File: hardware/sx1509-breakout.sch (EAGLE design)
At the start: 33 parts, among them U1 SX1509

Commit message: Adding silk around headers. Labeling SJ1.
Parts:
- removed JP11: (no value), SparkFun-Connectors:M111X11_NO_SILK
- added JP2: (no value), SparkFun-Connectors:M02PTH
- JP1: device SparkFun-Connectors:M021X02_NO_SILK -> SparkFun-Connectors:I2C_STANDARD
- JP3: device SparkFun-Connectors:I2C_STANDARD_NO_SILK -> SparkFun-Connectors:M11PTH
- JP4: value (none) -> IDC-5X2; device SparkFun-Connectors:M021X02_NO_SILK -> SparkFun-Connectors:M05X2SHD-NS
- JP5: value (none) -> IDC-5x2; device SparkFun-Connectors:I2C_STANDARD_NO_SILK -> SparkFun-Connectors:M05X2SHD-NS
- JP6: device SparkFun-Connectors:M111X11_NO_SILK -> SparkFun-Connectors:I2C_STANDARD
- JP7: value IDC-5X2 -> (none); device SparkFun-Connectors:M05X2SHD-NS -> SparkFun-Connectors:M02PTH
- JP8: value IDC-5x2 -> (none); device SparkFun-Connectors:M05X2SHD-NS -> SparkFun-Connectors:M11PTH
- SJ2, SJ3: value JUMPER-PAD-3-2OF3_NC_BY_TRACE_SMALL -> JUMPER-PAD-2-NC_BY_TRACE; device SparkFun-Passives:JUMPER-PAD-3-2OF3_NC_BY_TRACE_SMALL -> SparkFun-Passives:JUMPER-PAD-2-NC_BY_TRACE
- SJ4, SJ5: value JUMPER-PAD-2-NC_BY_TRACE -> JUMPER-PAD-3-2OF3_NC_BY_TRACE_SMALL; device SparkFun-Passives:JUMPER-PAD-2-NC_BY_TRACE -> SparkFun-Passives:JUMPER-PAD-3-2OF3_NC_BY_TRACE_SMALL
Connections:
- net !INT: now also JP2.2, R1.1; no longer JP4.2, R4.1
- net !RESET: now also JP2.1, JP7.1, R3.1; no longer JP1.1, JP4.1, R6.1
- net 0: now also JP3.4, JP5.1; no longer JP6.4, JP8.1
- net 1: now also JP3.5, JP5.2; no longer JP6.5, JP8.2
- net 10: now also JP4.3, JP8.9; no longer JP11.9, JP7.3
- net 11: now also JP4.4, JP8.8; no longer JP11.8, JP7.4
- net 12: now also JP4.7, JP8.7; no longer JP11.7, JP7.7
- net 13: now also JP4.8, JP8.6; no longer JP11.6, JP7.8
- net 14: now also JP4.9, JP8.5; no longer JP11.5, JP7.9
- net 15: now also JP4.10, JP8.4; no longer JP11.4, JP7.10
- net 2: now also JP3.6, JP5.3; no longer JP6.6, JP8.3
- net 3: now also JP3.7, JP5.4; no longer JP6.7, JP8.4
- net 3.3V: now also JP1.2, JP8.2, R1.2, R3.2, SJ2.2, SJ3.2; no longer JP11.2, JP5.2, R2.2, R4.2, SJ4.2, SJ5.2
- net 4: now also JP3.8, JP5.7; no longer JP6.8, JP8.7
- net 5: now also JP3.9, JP5.8; no longer JP6.9, JP8.8
- net 6: now also JP3.10, JP5.9; no longer JP6.10, JP8.9
- net 7: now also JP3.11, JP5.10; no longer JP6.11, JP8.10
- net 8: now also JP4.1, JP8.11; no longer JP11.11, JP7.1
- net 9: now also JP4.2, JP8.10; no longer JP11.10, JP7.2
- net ADDR0: now also SJ4.2; no longer SJ2.2
- net ADDR1: now also SJ5.2; no longer SJ3.2
- net GND: now also JP1.1, JP4.5, JP5.5, JP8.1, SJ4.3, SJ5.3; no longer JP11.1, JP5.1, JP7.5, JP8.5, SJ2.3, SJ3.3
- net N$1: now also R2.2; no longer R1.2
- net N$2: now also R4.2; no longer R3.2
- net N$8: now also R5.1, SJ4.1; no longer R2.1, SJ2.1
- net N$9: now also R6.1, SJ5.1; no longer R5.1, SJ3.1
- net OSCIO: now also JP7.2; no longer JP1.2
- net SCL: now also JP1.4, JP6.4, R2.1; no longer JP3.4, JP5.4, R1.1
- net SDA: now also JP1.3, JP6.3, R4.1; no longer JP3.3, JP5.3, R3.1
- net VCC1: now also JP3.3, JP5.6, SJ2.1; no longer JP6.3, JP8.6, SJ4.1
- net VCC2: now also JP4.6, JP8.3, SJ3.1; no longer JP11.3, JP7.6, SJ5.1
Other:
- note added: "SJ4 and SJ5 set the I2c address of the SX1509."
- note added: "The VCC1/2 jumpers (SJ2, SJ3) set those pins to 3.3V."
- note removed: "SJ2 and SJ3 set the I2c address of the SX1509."
- note removed: "The VCC1/2 jumpers (SJ4, SJ5) set those pins to 3.3V."
- moved on the sheet: R1, R2, R3, R4, R5, R6

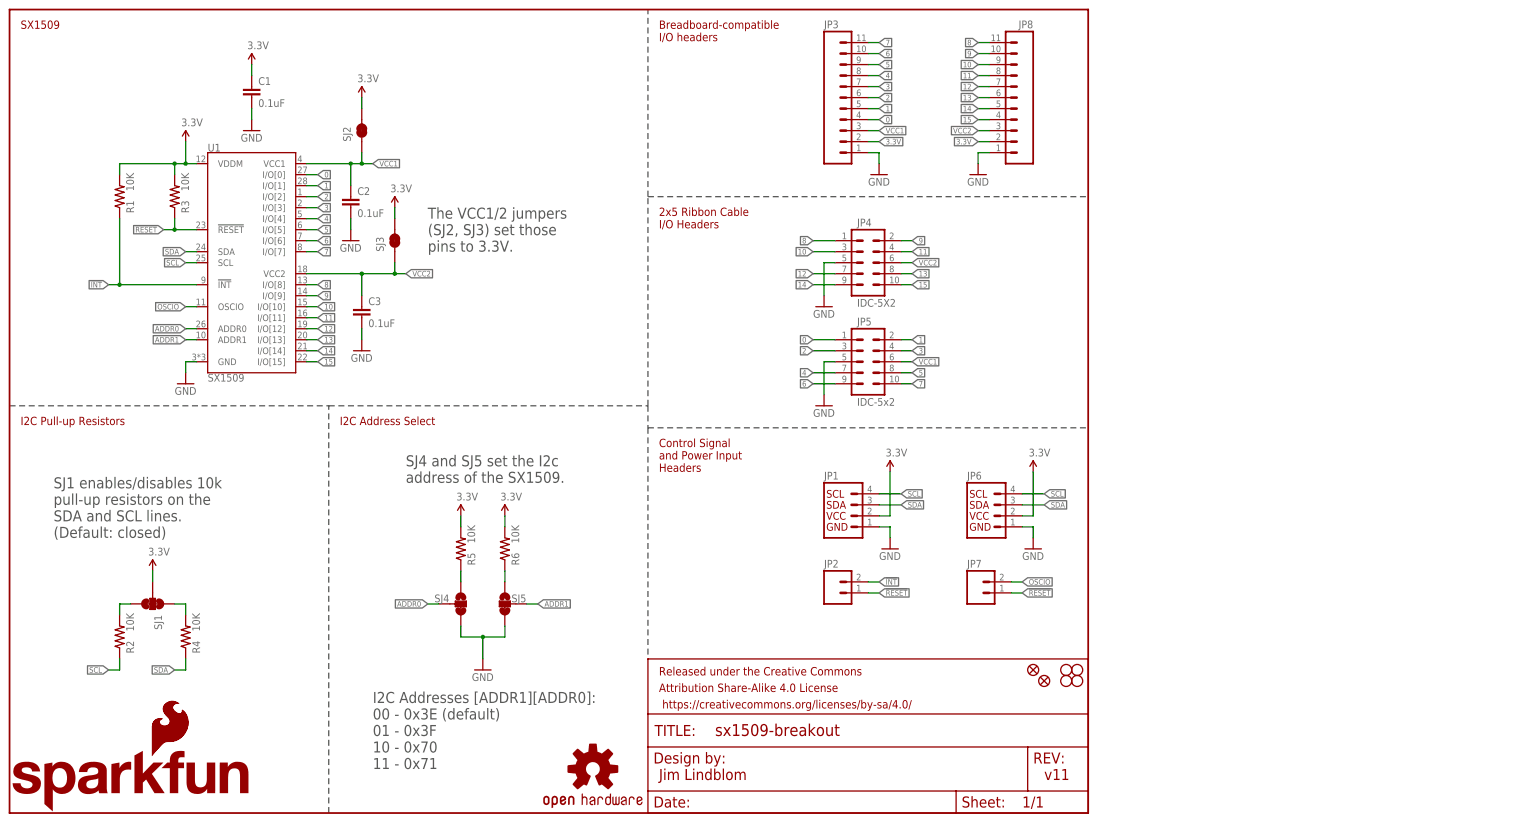
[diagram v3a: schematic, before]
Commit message: Revising GPIO headers to single 2x10 header.
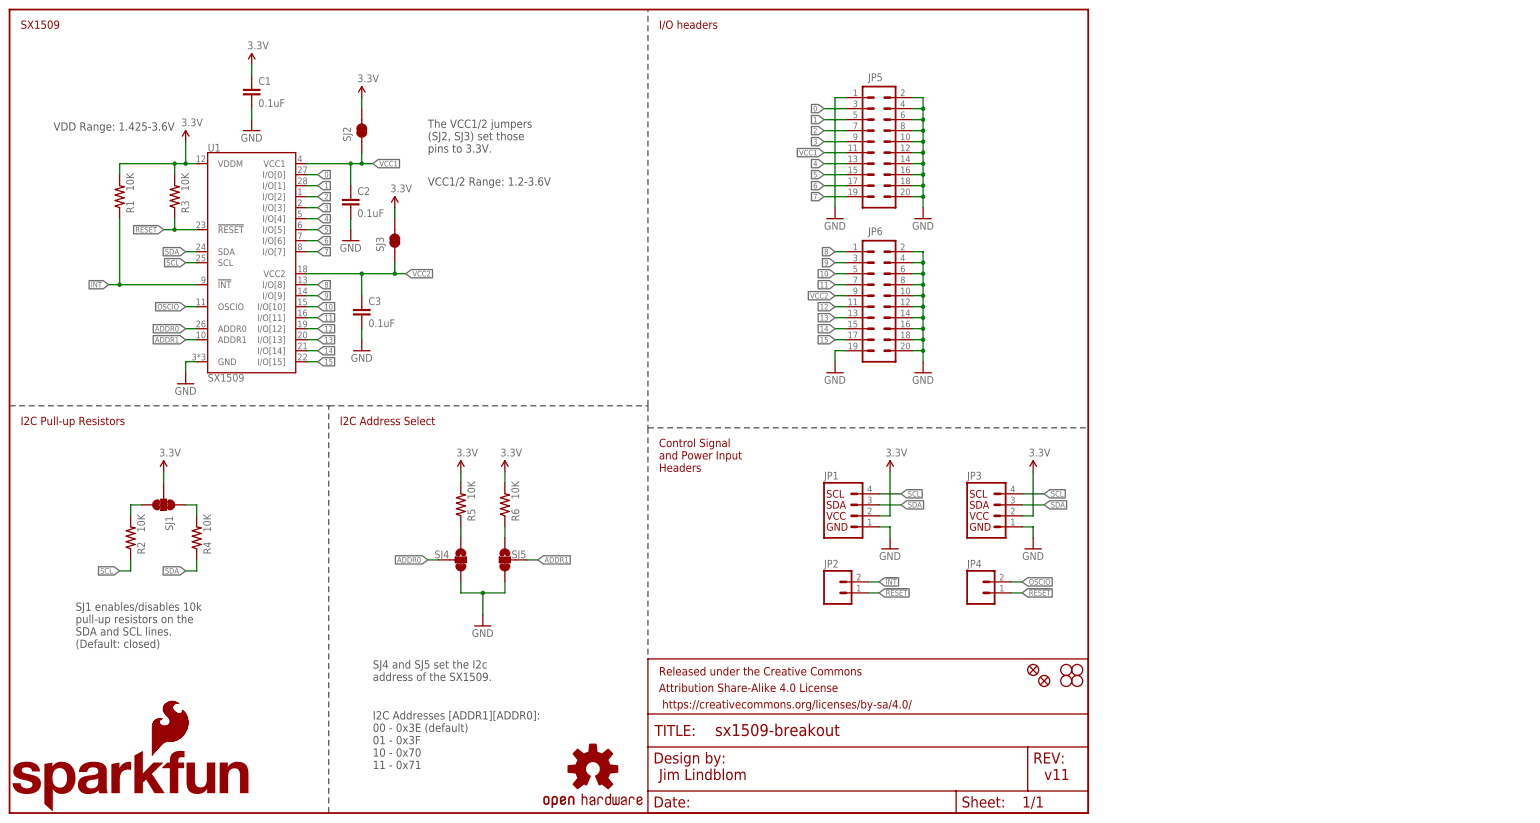
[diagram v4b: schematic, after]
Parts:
- removed JP7: (no value), SparkFun-Connectors:M02PTH
- removed JP8: (no value), SparkFun-Connectors:M11PTH
- JP3: device SparkFun-Connectors:M11PTH -> SparkFun-Connectors:I2C_STANDARD
- JP4: value IDC-5X2 -> (none); device SparkFun-Connectors:M05X2SHD-NS -> SparkFun-Connectors:M02PTH
- JP5: value IDC-5x2 -> (none); device SparkFun-Connectors:M05X2SHD-NS -> SparkFun-Connectors:M10X2NOSILK
- JP6: device SparkFun-Connectors:I2C_STANDARD -> SparkFun-Connectors:M10X2NOSILK
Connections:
- net !RESET: now also JP4.1; no longer JP7.1
- net 0: now also JP5.3; no longer JP3.4, JP5.1
- net 1: now also JP5.5; no longer JP3.5, JP5.2
- net 10: now also JP6.5; no longer JP4.3, JP8.9
- net 11: now also JP6.7; no longer JP4.4, JP8.8
- net 12: now also JP6.11; no longer JP4.7, JP8.7
- net 13: now also JP6.13; no longer JP4.8, JP8.6
- net 14: now also JP6.15; no longer JP4.9, JP8.5
- net 15: now also JP6.17; no longer JP4.10, JP8.4
- net 2: now also JP5.7; no longer JP3.6, JP5.3
- net 3: now also JP5.9; no longer JP3.7, JP5.4
- net 3.3V: no longer JP6.2, JP8.2
- net 4: now also JP5.13; no longer JP3.8, JP5.7
- net 5: now also JP5.15; no longer JP3.9, JP5.8
- net 6: now also JP5.17; no longer JP3.10, JP5.9
- net 7: now also JP5.19; no longer JP3.11, JP5.10
- net 8: now also JP6.1; no longer JP4.1, JP8.11
- net 9: now also JP6.3; no longer JP4.2, JP8.10
- net GND: now also JP5.1, JP5.10, JP5.12, JP5.14, JP5.16, JP5.18, JP5.2, JP5.20, JP5.4, JP5.6, JP5.8, JP6.10, JP6.12, JP6.14, JP6.16, JP6.18, JP6.19, JP6.2, JP6.20, JP6.4, JP6.6, JP6.8; no longer JP4.5, JP5.5, JP6.1, JP8.1
- net OSCIO: now also JP4.2; no longer JP7.2
- net SCL: now also JP3.4; no longer JP6.4
- net SDA: now also JP3.3; no longer JP6.3
- net VCC1: now also JP5.11; no longer JP3.3, JP5.6
- net VCC2: now also JP6.9; no longer JP4.6, JP8.3
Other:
- note added: "I/O headers"
- note added: "VCC1/2 Range: 1.2-3.6V"
- note added: "VDD Range: 1.425-3.6V"
- note removed: "2x5 Ribbon Cable I/O Headers"
- note removed: "Breadboard-compatible I/O headers"
- moved on the sheet: R2, R4, R5, R6, SJ1, SJ4, SJ5
